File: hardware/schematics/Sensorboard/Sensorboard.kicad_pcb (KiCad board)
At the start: 2 copper layers, 138 x 76 mm, 59 parts, among them J1 Grauwasser, J2 BNO055 IMU, J3 BME680 #0 Innen, J4 RS485, J5 BME680 #1 Außen, J6 HX711 GasWaage, J7 LT452 Malibu, J8 Frischwasser, Q1 BSS138, Q2 BSS138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

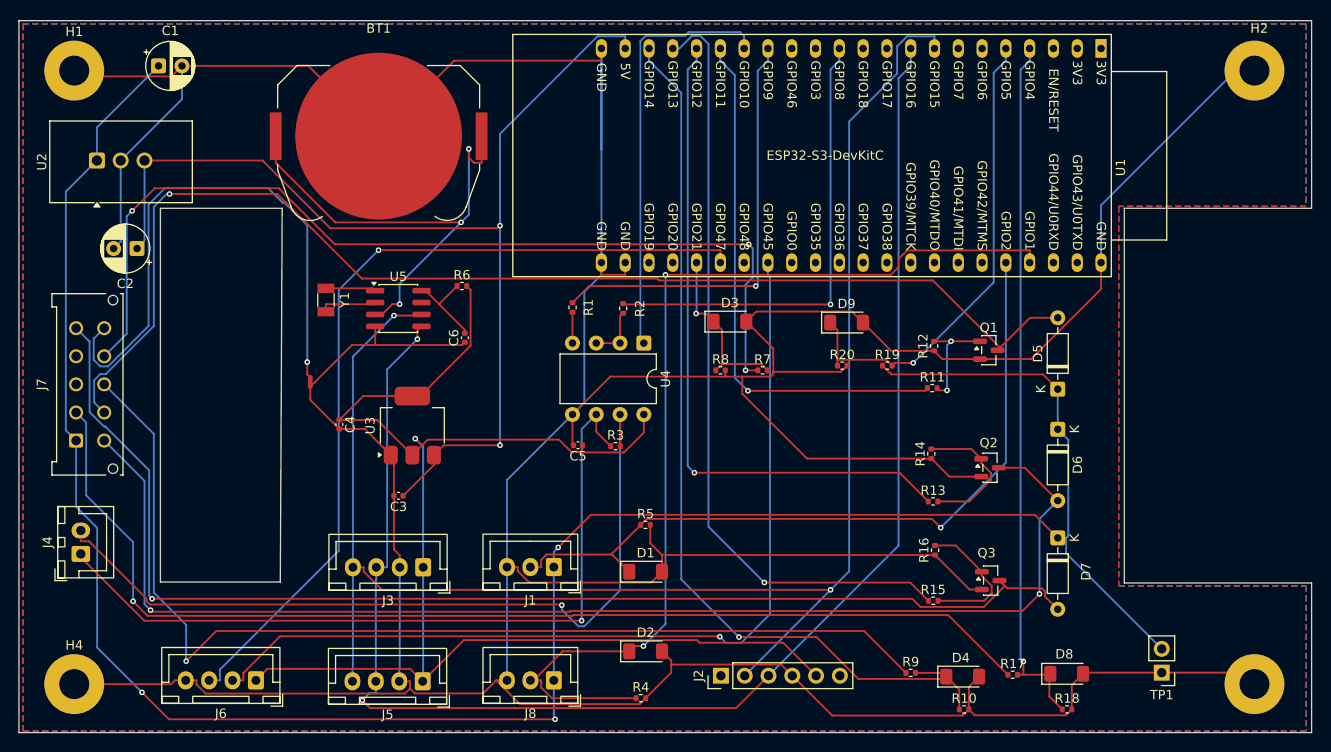
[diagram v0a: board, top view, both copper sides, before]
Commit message: hw(sensorboard): KiCad Schaltplan + Gerber aktualisiert
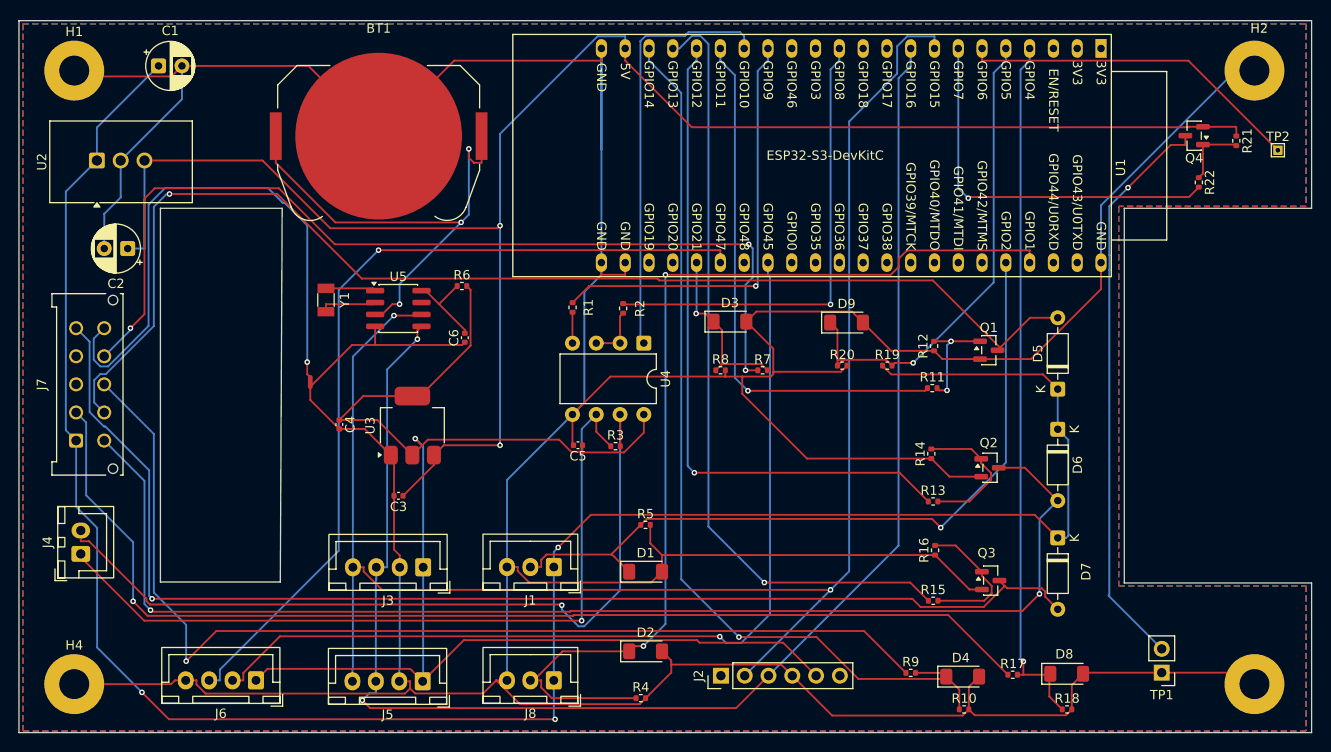
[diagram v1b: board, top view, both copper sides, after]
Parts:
- added Q4: AO3401A, Package_TO_SOT_SMD:SOT-23, F.Cu at (195.6, 56.5)
- added R21: 100k, Resistor_SMD:R_0402_1005Metric, F.Cu at (200.1, 57.0)
- added R22: 10k, Resistor_SMD:R_0402_1005Metric, F.Cu at (196.1, 61.4)
- added TP2: Display Touch, TestPoint:TestPoint_THTPad_1.0x1.0mm_Drill0.5mm, F.Cu at (204.5, 58.0)
- moved C2 1.00 mm to (81.7, 68.5)
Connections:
- TP1 pad 2: /WB -> Net-(Q4-D)
- U1 pad 6: unconnected-(U1-GPIO6/ADC1_CH5-Pad6) -> Net-(U1-GPIO6/ADC1_CH5)
- U1 pad 7: unconnected-(U1-GPIO7/ADC1_CH6-Pad7) -> Net-(U1-GPIO7/ADC1_CH6)
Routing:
- net /+5V: track 116.2 -> 188.6 mm
- net Net-(Q4-D): track 0.00 -> 61.4 mm, vias 0 -> 1
- net Net-(U1-GPIO7/ADC1_CH6): track 0.00 -> 41.5 mm, vias 0 -> 1
- net Net-(U1-GPIO6/ADC1_CH5): track 0.00 -> 36.8 mm
- net /WB: track 247.2 -> 231.1 mm
- net Net-(Q4-G): track 0.00 -> 7.32 mm
- net Net-(D9-K): track 51.1 -> 51.9 mm
- net Net-(J4-Pin_2): track 87.7 -> 87.2 mm

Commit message: hardware(kicad): Sensorboard Rev 1.0 – Schematic/PCB aktualisiert, Produktionsdateien aus Tracking entfernt
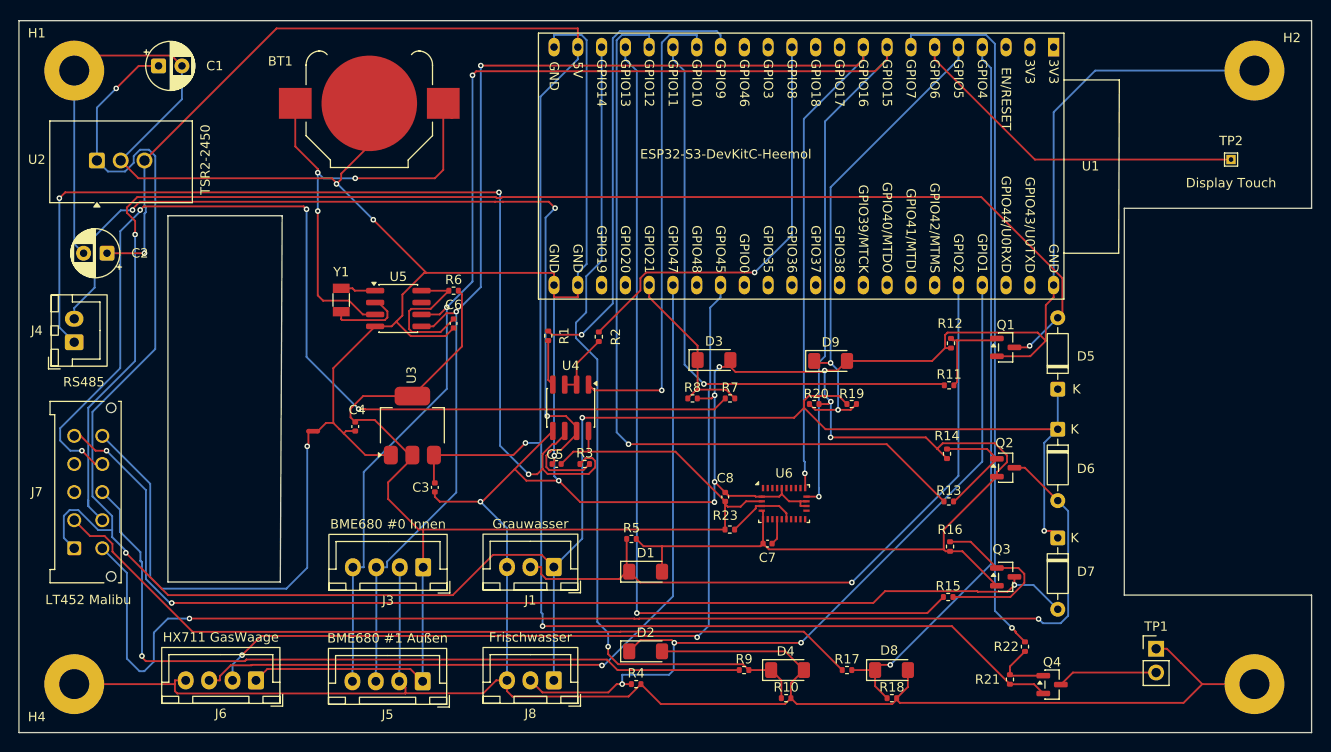
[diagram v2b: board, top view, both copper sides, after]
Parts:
- removed J2: BNO055 IMU, Connector_PinHeader_2.54mm:PinHeader_1x06_P2.54mm_Vertical
- added C7: 1uF, Capacitor_SMD:C_0402_1005Metric, F.Cu at (150.0, 100.0)
- added C8: 100nF, Capacitor_SMD:C_0402_1005Metric, F.Cu at (145.5, 95.0)
- added R23: 10k, Resistor_SMD:R_0402_1005Metric, F.Cu at (146.0, 98.5)
- added U6: BNO055, Package_LGA:LGA-28_5.2x3.8mm_P0.5mm, F.Cu at (151.8, 95.7)
- BT1: footprint Battery:BatteryHolder_Keystone_3034_1x20mm -> Battery:BatteryHolder_Keystone_3000_1x12mm
- U1: value ESP32-S3-DevKitC -> ESP32-S3-DevKitC-Heemol; footprint PCM_Espressif:ESP32-S3-DevKitC -> PCM_Espressif:ESP32-S3-DevKitC-Heemol
- U4: footprint Package_DIP:DIP-8_W7.62mm -> Package_SO:SOIC-8_3.9x4.9mm_P1.27mm
- moved R21 62.4 mm to (175.9, 114.5), turned to 90 degrees
- moved Q4 60.5 mm to (180.4, 115.0), turned to 0 degrees
- moved R22 52.9 mm to (177.5, 111.0), turned to 90 degrees
- moved J4 22.6 mm to (76.0, 78.5)
- moved R10 19.0 mm to (152.0, 116.5)
- moved R18 18.7 mm to (163.3, 116.5)
- moved D4 18.7 mm to (152.2, 113.5)
- moved D8 18.7 mm to (163.2, 113.5)
- moved R9 17.8 mm to (147.5, 113.5)
- moved R17 17.7 mm to (158.5, 113.5)
- moved J7 11.5 mm to (76.0, 100.5)
- moved U4 10.4 mm to (129.0, 85.5)
- moved R19 5.59 mm to (159.0, 85.1)
- moved NT1 5.26 mm to (101.5, 88.0), turned to 0 degrees
- moved TP2 5.10 mm to (199.5, 59.0)
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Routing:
- net GND: track 587.4 -> 656.7 mm, vias 0 -> 12
- net Net-(Q4-D): track 61.4 -> 10.7 mm, vias 1 -> 0
- net Net-(U1-GPIO7/ADC1_CH6): track 41.5 -> 75.8 mm
- net /SB: track 119.4 -> 89.1 mm, vias 1 -> 0
- net /12V - Kontrolle: track 113.2 -> 84.6 mm
- net Net-(J4-Pin_1): track 83.3 -> 110.4 mm, vias 1 -> 3
- net Net-(D2-K): track 108.2 -> 86.7 mm, vias 2 -> 3
- net /12V - EIN: track 130.9 -> 151.4 mm, vias 1 -> 2
- net +3.3V: track 154.2 -> 137.9 mm, vias 1 -> 0
- net /+5V: track 188.6 -> 204.9 mm, vias 2 -> 3
- net /Netz: track 101.3 -> 115.0 mm, vias 3 -> 4
- net Net-(U1-GPIO12/ADC2_CH1): track 72.2 -> 84.9 mm
- net /Multimedia: track 132.5 -> 120.7 mm, vias 1 -> 3
- net Net-(U1-GPIO13/ADC2_CH2): track 83.0 -> 94.4 mm
- net Net-(J4-Pin_2): track 87.2 -> 98.3 mm, vias 1 -> 3
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- removed copper zone on B.Cu, net GND
- removed copper zone on F.Cu, net GND
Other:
- outline, holes or cut-outs redrawn

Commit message: hardware(sensorboard): Zwei neue 12V-Schaltausgänge (Pumpe, Licht) hinzugefügt, Aufräumen und Fehler des Vorgänger-Boards behoben
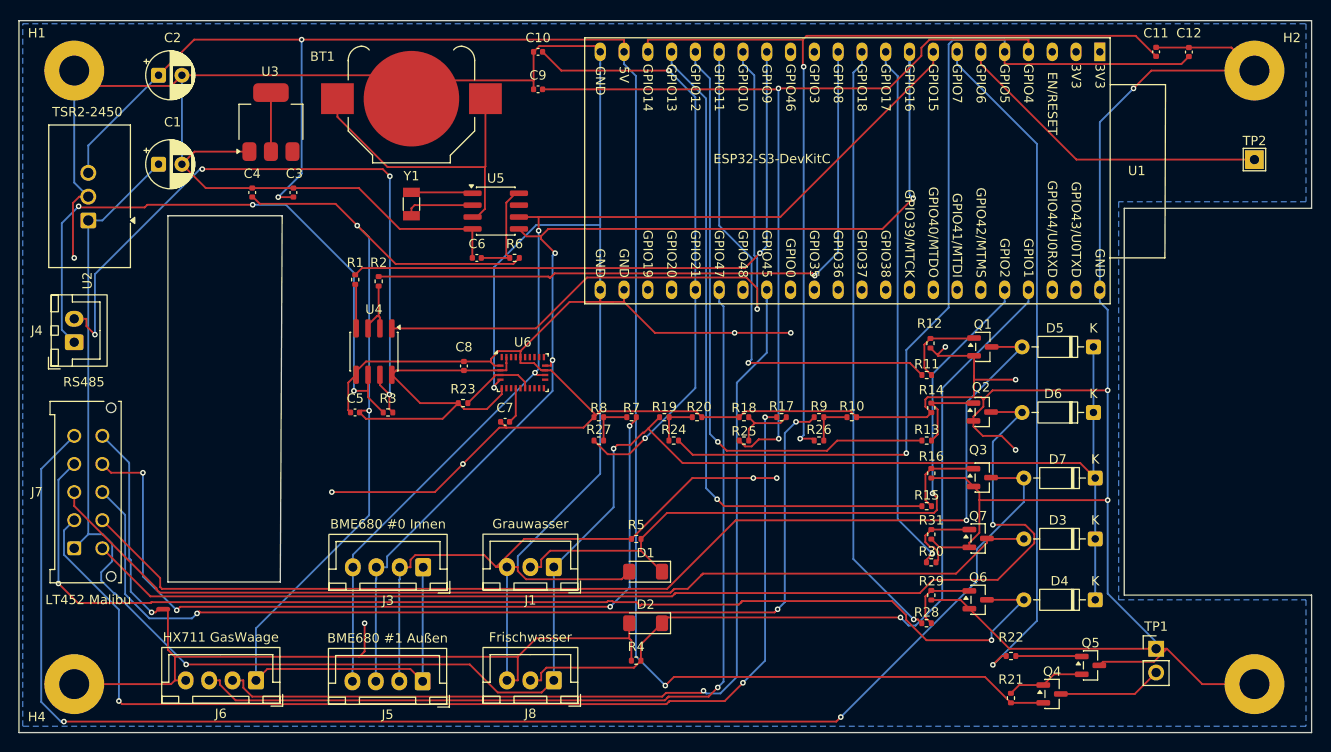
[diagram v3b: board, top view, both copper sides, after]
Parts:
- removed D8, D9: BZV55B3V3, Diode_SMD:D_MiniMELF
- added C10: 100nF, Capacitor_SMD:C_0402_1005Metric, F.Cu at (125.5, 47.5)
- added C11: 100nF, Capacitor_SMD:C_0402_1005Metric, F.Cu at (191.5, 47.5)
- added C12: 100nF, Capacitor_SMD:C_0402_1005Metric, F.Cu at (195.0, 47.5)
- added C9: 100nF, Capacitor_SMD:C_0402_1005Metric, F.Cu at (125.5, 51.5)
- added Q5: 2N7002, Package_TO_SOT_SMD:SOT-23, F.Cu at (184.5, 113.0)
- added Q6: BSS138, Package_TO_SOT_SMD:SOT-23, F.Cu at (172.5, 106.0)
- added Q7: BSS138, Package_TO_SOT_SMD:SOT-23, F.Cu at (172.5, 99.5)
- added R24: 1k, Resistor_SMD:R_0402_1005Metric, F.Cu at (140.0, 89.0)
- added R25: 1k, Resistor_SMD:R_0402_1005Metric, F.Cu at (147.5, 89.0)
- added R26: 1k, Resistor_SMD:R_0402_1005Metric, F.Cu at (155.5, 89.0)
- added R27: 1k, Resistor_SMD:R_0402_1005Metric, F.Cu at (132.0, 89.0)
- added R28: 100, Resistor_SMD:R_0402_1005Metric, F.Cu at (167.0, 108.5)
- added R29: 100k, Resistor_SMD:R_0402_1005Metric, F.Cu at (167.5, 105.5)
- added R30: 100, Resistor_SMD:R_0402_1005Metric, F.Cu at (167.5, 102.0)
- added R31: 100k, Resistor_SMD:R_0402_1005Metric, F.Cu at (167.5, 99.0)
- D3, D4: value BZV55B3V3 -> 1N4148; footprint Diode_SMD:D_MiniMELF -> Diode_THT:D_DO-35_SOD27_P7.62mm_Horizontal
- TP2: footprint TestPoint:TestPoint_THTPad_1.0x1.0mm_Drill0.5mm -> TestPoint:TestPoint_THTPad_2.0x2.0mm_Drill1.0mm
- U1: value ESP32-S3-DevKitC-Heemol -> ESP32-S3-DevKitC
- moved D3 45.0 mm to (185.0, 99.5), turned to 180 degrees
- moved U3 35.7 mm to (97.0, 55.0)
- moved C3 34.9 mm to (99.4, 62.5), turned to 90 degrees
- moved R18 33.9 mm to (147.5, 86.5), turned to 180 degrees
- moved D4 33.7 mm to (185.0, 106.0), turned to 180 degrees
- moved R23 31.5 mm to (117.5, 85.0)
- moved C8 31.2 mm to (117.6, 81.0)
- moved U6 31.2 mm to (123.9, 81.8)
- moved C7 30.9 mm to (122.0, 87.0)
- moved R10 30.8 mm to (159.0, 86.5)
- moved R9 28.2 mm to (155.5, 86.5)
- moved R17 27.9 mm to (151.5, 86.5)
- moved C4 27.3 mm to (95.0, 62.5), turned to 90 degrees
- moved NT1 24.8 mm to (85.5, 107.0)
- moved R2 24.2 mm to (108.5, 72.0)
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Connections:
- D3 pad 1: Net-(D3-K) -> /WB
- D3 pad 2: GND -> /Licht
- D4 pad 1: Net-(D4-K) -> /WB
- D4 pad 2: GND -> /Pumpe
- J7 pad 3: unconnected-(J7-Pin_3-Pad3) -> /Licht
- J7 pad 4: unconnected-(J7-Pin_4-Pad4) -> /Pumpe
- R10 pad 1: Net-(D4-K) -> Net-(R10-Pad1)
- R17 pad 2: Net-(D8-K) -> Net-(R17-Pad2)
- R18 pad 1: Net-(D8-K) -> Net-(R17-Pad2)
- R19 pad 2: Net-(D9-K) -> Net-(R19-Pad2)
- R20 pad 1: Net-(D9-K) -> Net-(R19-Pad2)
- R22 pad 1: Net-(Q4-G) -> Net-(Q5-G)
- R7 pad 2: Net-(D3-K) -> Net-(R27-Pad2)
- R8 pad 1: Net-(D3-K) -> Net-(R27-Pad2)
- R9 pad 2: Net-(D4-K) -> Net-(R10-Pad1)
- U1 pad 10: unconnected-(U1-GPIO17/ADC2_CH6-Pad10) -> Net-(U1-GPIO17/ADC2_CH6)
- U1 pad 11: unconnected-(U1-GPIO18/ADC2_CH7-Pad11) -> Net-(U1-GPIO18/ADC2_CH7)
- U1 pad 20: Net-(D4-K) -> Net-(U1-GPIO14/ADC2_CH3)
- U1 pad 27: Net-(D3-K) -> Net-(U1-GPIO21)
- U1 pad 4: Net-(D8-K) -> Net-(U1-GPIO4/ADC1_CH3)
- U1 pad 5: Net-(D9-K) -> Net-(U1-GPIO5/ADC1_CH4)
- U3 pad 2: +3.3V -> unconnected-(U3-VO-Pad2)
- U3 pad 3: /+5V -> unconnected-(U3-VI-Pad3)
- U6 pad 17: GND -> /I2C SCL
- U6 pad 19: /I2C SCL -> /I2C SDA
- U6 pad 20: /I2C SDA -> unconnected-(U6-COM0-Pad20)
- U6 pad 28: unconnected-(U6-VDDIO-Pad28) -> +3.3V
- U6 pad 6: GND -> +3.3V
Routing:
- net /Pumpe: track 0.00 -> 126.7 mm, vias 0 -> 2
- net /Licht: track 0.00 -> 109.9 mm
- net Net-(U1-GPIO14/ADC2_CH3): track 0.00 -> 101.0 mm, vias 0 -> 2
- net Net-(U1-GPIO5/ADC1_CH4): track 0.00 -> 100.6 mm, vias 0 -> 1
- net Net-(U1-GPIO4/ADC1_CH3): track 0.00 -> 98.1 mm, vias 0 -> 2
- net GND: track 656.7 -> 753.4 mm, vias 12 -> 15
- net Net-(D4-K): track 88.9 -> 0.00 mm, vias 1 -> 0
- net Net-(D8-K): track 78.7 -> 0.00 mm, vias 1 -> 0
- net Net-(U1-GPIO18/ADC2_CH7): track 0.00 -> 64.7 mm, vias 0 -> 1
- net Net-(U1-GPIO21): track 0.00 -> 63.7 mm, vias 0 -> 2
- net /I2C SCL: track 172.3 -> 111.9 mm, vias 3 -> 2
- net Net-(U1-GPIO17/ADC2_CH6): track 0.00 -> 57.5 mm, vias 0 -> 1
- net Net-(D9-K): track 52.1 -> 0.00 mm, vias 2 -> 0
- net /I2C SDA: track 167.6 -> 119.7 mm
- net Net-(J4-Pin_1): track 110.4 -> 67.2 mm
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- added copper zone on B.Cu, net GND
